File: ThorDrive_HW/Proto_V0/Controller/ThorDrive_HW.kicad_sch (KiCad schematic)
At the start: 33 parts, among them J1 Conn_01x04_Socket, J2 Conn_01x06_Socket, J3 Conn_01x03_Socket, J4 Conn_01x08_Socket, J5 Conn_01x08_Pin, J6 Conn_01x04_Pin, J7 Conn_01x06_Pin, J8 Conn_01x04_Pin, J9 Conn_01x04_Pin, SW1 SW_Push, U1 ATmega328P-P, U4 7400, Y1 Crystal, Y2 Crystal

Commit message: update
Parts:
- C1, C2, C7: footprint (none) -> Capacitor_SMD:C_0805_2012Metric_Pad1.18x1.45mm_HandSolder
- D1, D2, D3, D4, D5, D6: footprint (none) -> LED_SMD:LED_1206_3216Metric_Pad1.42x1.75mm_HandSolder
- R1, R2: footprint (none) -> Resistor_SMD:R_1206_3216Metric_Pad1.30x1.75mm_HandSolder
- R10, R11, R12, R13, R14, R15: footprint (none) -> Resistor_SMD:R_0805_2012Metric_Pad1.20x1.40mm_HandSolder
- U4: footprint (none) -> Package_SO:SOIC-14_3.9x8.7mm_P1.27mm
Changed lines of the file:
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@@
 			)
 		)
-		(property "Footprint" ""
+		(property "Footprint" "Resistor_SMD:R_1206_3216Metric_Pad1.30x1.75mm_HandSolder"
 			(at 92.202 62.23 90)
 			(effects
@@
 			)
 		)
-		(property "Footprint" ""
+		(property "Footprint" "Capacitor_SMD:C_0805_2012Metric_Pad1.18x1.45mm_HandSolder"
 			(at 26.3652 39.37 0)
 			(effects
@@
 			)
 		)
-		(property "Footprint" ""
+		(property "Footprint" "Resistor_SMD:R_0805_2012Metric_Pad1.20x1.40mm_HandSolder"
 			(at 80.772 27.94 90)
 			(effects
@@
 			)
 		)
-		(property "Footprint" ""
+		(property "Footprint" "Capacitor_SMD:C_0805_2012Metric_Pad1.18x1.45mm_HandSolder"
 			(at 134.62 49.8348 0)
 			(effects
@@
 			)
 		)
-		(property "Footprint" ""
+		(property "Footprint" "Package_SO:SOIC-14_3.9x8.7mm_P1.27mm"
 			(at 53.34 154.94 0)
 			(effects
@@
 			)
 		)
-		(property "Footprint" ""
+		(property "Footprint" "LED_SMD:LED_1206_3216Metric_Pad1.42x1.75mm_HandSolder"
 			(at 154.94 43.18 0)
 			(effects
@@
 			)
 		)
-		(property "Footprint" ""
+		(property "Footprint" "Package_SO:SOIC-14_3.9x8.7mm_P1.27mm"
 			(at 53.34 115.57 0)
 			(effects
@@
 			)
 		)
-		(property "Footprint" ""
+		(property "Footprint" "LED_SMD:LED_1206_3216Metric_Pad1.42x1.75mm_HandSolder"
 			(at 161.29 43.18 0)
 			(effects
@@
 			)
 		)
-		(property "Footprint" ""
+		(property "Footprint" "Resistor_SMD:R_1206_3216Metric_Pad1.30x1.75mm_HandSolder"
 			(at 94.742 45.72 90)
 			(effects
@@
 			)
 		)
-		(property "Footprint" ""
+		(property "Footprint" "Resistor_SMD:R_0805_2012Metric_Pad1.20x1.40mm_HandSolder"
 			(at 275.082 39.37 90)
 			(effects
@@
 			)
 		)
-		(property "Footprint" ""
+		(property "Footprint" "LED_SMD:LED_1206_3216Metric_Pad1.42x1.75mm_HandSolder"
 			(at 82.55 35.56 0)
 			(effects
@@
 			)
 		)
-		(property "Footprint" ""
+		(property "Footprint" "Package_SO:SOIC-14_3.9x8.7mm_P1.27mm"
 			(at 53.34 142.24 0)
 			(effects
@@
 			)
 		)
-		(property "Footprint" ""
+		(property "Footprint" "Resistor_SMD:R_0805_2012Metric_Pad1.20x1.40mm_HandSolder"
 			(at 153.162 34.29 90)
 			(effects
@@
 			)
 		)
-		(property "Footprint" ""
+		(property "Footprint" "Capacitor_SMD:C_0805_2012Metric_Pad1.18x1.45mm_HandSolder"
 			(at 134.62 39.6748 0)
 			(effects
@@
 			)
 		)
-		(property "Footprint" ""
+		(property "Footprint" "Resistor_SMD:R_0805_2012Metric_Pad1.20x1.40mm_HandSolder"
 			(at 159.512 34.29 90)
 			(effects
@@
 			)
 		)
-		(property "Footprint" ""
+		(property "Footprint" "Resistor_SMD:R_0805_2012Metric_Pad1.20x1.40mm_HandSolder"
 			(at 159.512 72.39 90)
 			(effects
@@
 			)
 		)
-		(property "Footprint" ""
+		(property "Footprint" "Package_SO:SOIC-14_3.9x8.7mm_P1.27mm"
 			(at 53.34 129.54 0)
 			(effects
@@
 			)
 		)
-		(property "Footprint" ""
+		(property "Footprint" "LED_SMD:LED_1206_3216Metric_Pad1.42x1.75mm_HandSolder"
 			(at 161.29 80.01 0)
 			(effects
@@
 			)
 		)
-		(property "Footprint" ""
+		(property "Footprint" "LED_SMD:LED_1206_3216Metric_Pad1.42x1.75mm_HandSolder"
 			(at 147.32 43.18 0)
 			(effects
@@
 			)
 		)
-		(property "Footprint" ""
+		(property "Footprint" "LED_SMD:LED_1206_3216Metric_Pad1.42x1.75mm_HandSolder"
 			(at 276.86 48.26 0)
 			(effects
@@
 			)
 		)
-		(property "Footprint" ""
+		(property "Footprint" "Resistor_SMD:R_0805_2012Metric_Pad1.20x1.40mm_HandSolder"
 			(at 145.542 34.29 90)
 			(effects
@@
 			)
 		)
-		(property "Footprint" ""
+		(property "Footprint" "Package_SO:SOIC-14_3.9x8.7mm_P1.27mm"
 			(at 261.62 44.45 0)
 			(effects

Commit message: Routing Try0
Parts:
- removed RV1: R_Potentiometer, symbol Device:R_Potentiometer
- added J10: Conn_01x03_Socket, Connector_JST:JST_EH_B3B-EH-A_1x03_P2.50mm_Vertical, symbol Connector:Conn_01x03_Socket
- J1: footprint (none) -> Connector_JST:JST_EH_B4B-EH-A_1x04_P2.50mm_Vertical
- J2: footprint (none) -> Connector_JST:JST_EH_B6B-EH-A_1x06_P2.50mm_Vertical
- J3: footprint (none) -> Connector_JST:JST_EH_B3B-EH-A_1x03_P2.50mm_Vertical
- J4: footprint (none) -> Connector_JST:JST_EH_B8B-EH-A_1x08_P2.50mm_Vertical
- J5: footprint (none) -> Connector_PinHeader_2.54mm:PinHeader_1x08_P2.54mm_Vertical
- J6, J8, J9: footprint (none) -> Connector_PinHeader_2.54mm:PinHeader_1x04_P2.54mm_Vertical
- J7: footprint (none) -> Connector_PinHeader_2.54mm:PinHeader_1x06_P2.54mm_Vertical
- RV2: footprint (none) -> Potentiometer_THT:Potentiometer_Piher_T-16H_Single_Horizontal
- SW1: footprint (none) -> libMain:SW_BUTT-2
- Y1: footprint (none) -> Crystal:Crystal_SMD_HC49-SD_HandSoldering
- Y2: footprint (none) -> Crystal:Crystal_HC49-4H_Vertical
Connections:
- net +5V: now also D2.2 (A), D3.2 (A), D4.2 (A), D5.2 (A), D6.2 (A), J10.3 (Pin_3); no longer R11.1, R12.1, R13.1, R14.1, R15.1
- net Fault: now also R15.2; no longer D6.1 (K)
- net GND: now also R14.2, J10.1 (Pin_1); no longer D5.1 (K)
- net HallA: now also R13.2; no longer D2.1 (K)
- net HallB: now also R12.2; no longer D4.1 (K)
- net HallC: now also R11.2; no longer D3.1 (K)
- net pot: now also J10.2 (Pin_2)
- new net: D4.1 (K), R12.1
- new net: D3.1 (K), R11.1
- new net: D5.1 (K), R14.1
- new net: D6.1 (K), R15.1
- new net: D2.1 (K), R13.1
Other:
- moved on the sheet: D2, D3, D4, D5, D6, R11, R12, R13, R14, R15

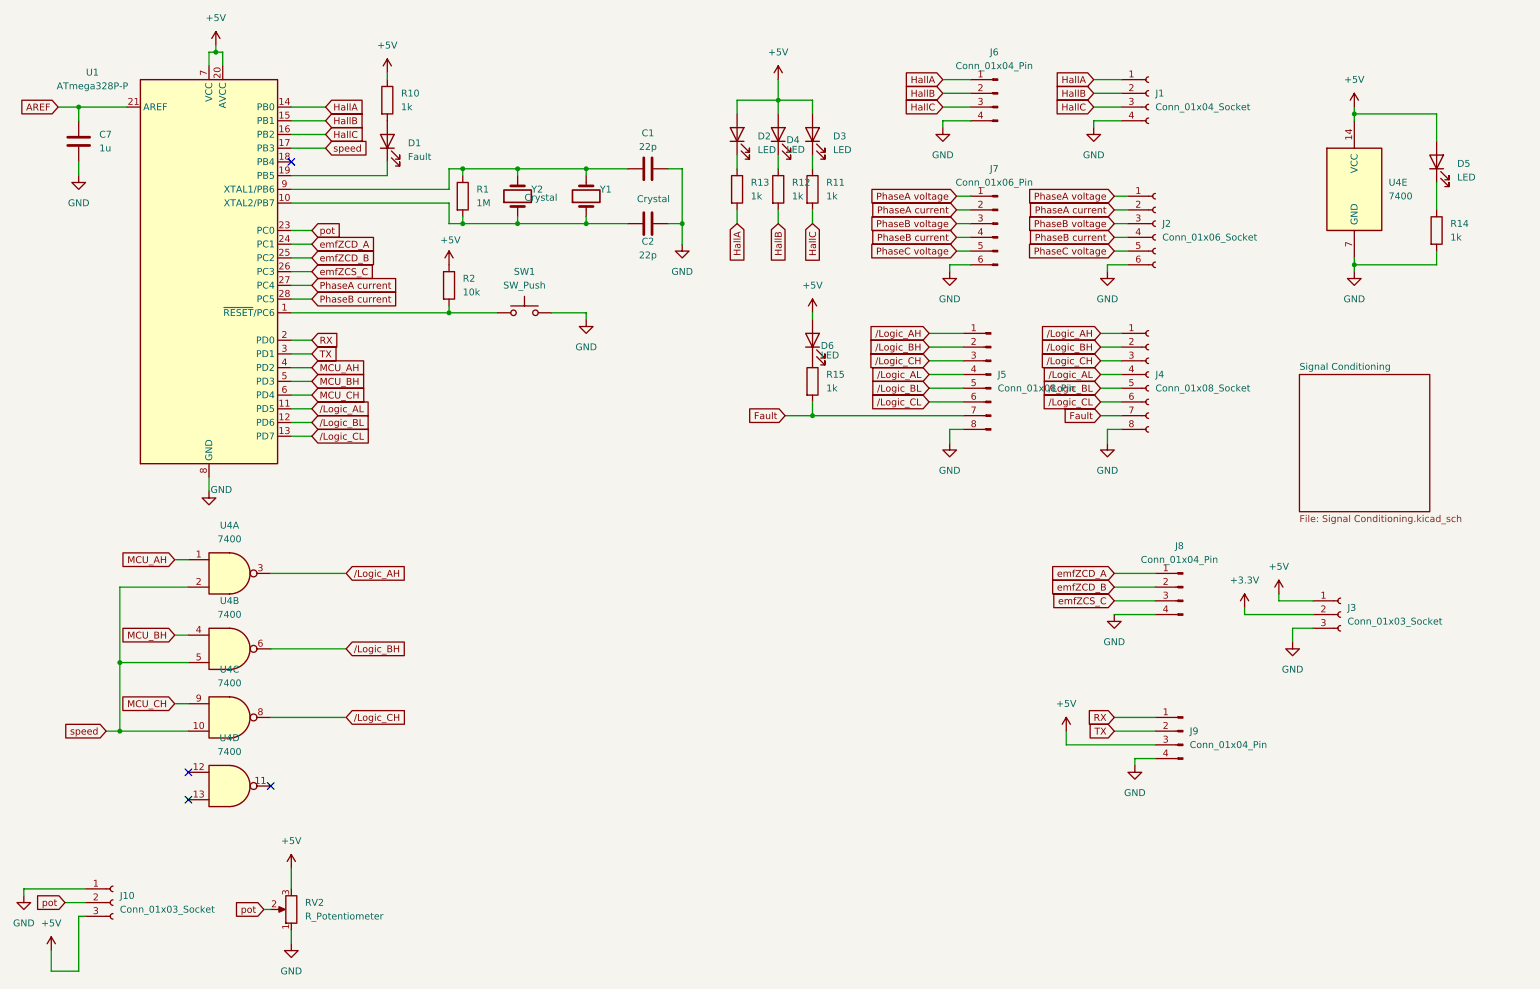
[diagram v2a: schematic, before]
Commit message: Controller Board V0 Finalized
A Controller Board simple and built upon the Atmega328p...
Single Layer Design with few jumpers.... Compatible with Inverter V0
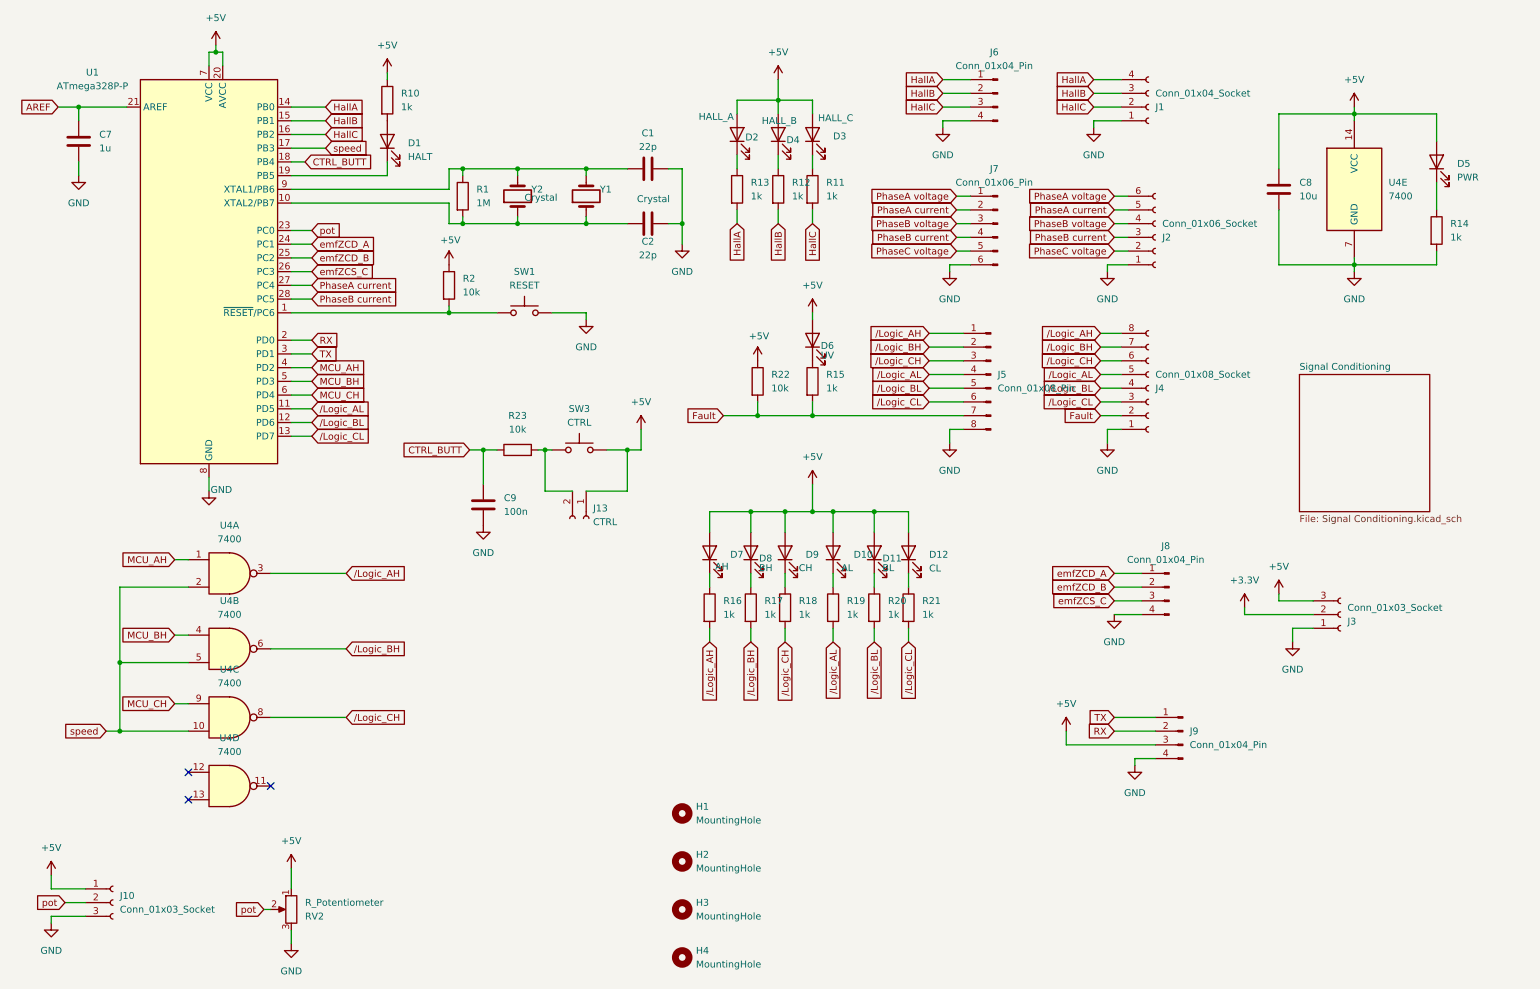
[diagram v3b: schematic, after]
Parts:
- added C8: 10u, Capacitor_SMD:C_0805_2012Metric_Pad1.18x1.45mm_HandSolder, symbol Device:C
- added C9: 100n, Capacitor_SMD:C_0805_2012Metric_Pad1.18x1.45mm_HandSolder, symbol Device:C
- added D10: AL, LED_THT:LED_D3.0mm, symbol Device:LED
- added D11: BL, LED_THT:LED_D3.0mm, symbol Device:LED
- added D12: CL, LED_THT:LED_D3.0mm, symbol Device:LED
- added D7: AH, LED_THT:LED_D3.0mm, symbol Device:LED
- added D8: BH, LED_THT:LED_D3.0mm, symbol Device:LED
- added D9: CH, LED_THT:LED_D3.0mm, symbol Device:LED
- added H1, H2, H3, H4: MountingHole, MountingHole:MountingHole_3.2mm_M3, symbol Mechanical:MountingHole
- added J13: CTRL, Connector_JST:JST_EH_B2B-EH-A_1x02_P2.50mm_Vertical, symbol Connector:Conn_01x02_Socket
- added R16, R17, R18, R19, R20, R21: 1k, Resistor_SMD:R_0805_2012Metric_Pad1.20x1.40mm_HandSolder, symbol Device:R
- added R22, R23: 10k, Resistor_SMD:R_1206_3216Metric_Pad1.30x1.75mm_HandSolder, symbol Device:R
- added SW3: CTRL, libMain:SW_BUTT-2, symbol Switch:SW_Push
- D1: value Fault -> HALT; footprint LED_SMD:LED_1206_3216Metric_Pad1.42x1.75mm_HandSolder -> LED_THT:LED_D3.0mm
- D2: value LED -> HALL_A; footprint LED_SMD:LED_1206_3216Metric_Pad1.42x1.75mm_HandSolder -> LED_THT:LED_D3.0mm
- D3: value LED -> HALL_C; footprint LED_SMD:LED_1206_3216Metric_Pad1.42x1.75mm_HandSolder -> LED_THT:LED_D3.0mm
- D4: value LED -> HALL_B; footprint LED_SMD:LED_1206_3216Metric_Pad1.42x1.75mm_HandSolder -> LED_THT:LED_D3.0mm
- D5: value LED -> PWR; footprint LED_SMD:LED_1206_3216Metric_Pad1.42x1.75mm_HandSolder -> LED_THT:LED_D3.0mm
- D6: value LED -> UV; footprint LED_SMD:LED_1206_3216Metric_Pad1.42x1.75mm_HandSolder -> LED_THT:LED_D3.0mm
- SW1: value SW_Push -> RESET
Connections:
- net +5V: now also J10.1 (Pin_1), J3.3 (Pin_3), RV2.1, C8.1, D10.2 (A), D11.2 (A), D12.2 (A), D7.2 (A), D8.2 (A), D9.2 (A), J13.1 (Pin_1), R22.1, SW3.2; no longer J10.3 (Pin_3), J3.1 (Pin_1), RV2.3
- net Fault: now also J4.2 (Pin_2), R22.2; no longer J4.7 (Pin_7)
- net GND: now also J1.1 (Pin_1), J10.3 (Pin_3), J2.1 (Pin_1), J3.1 (Pin_1), J4.1 (Pin_1), RV2.3, C8.2, C9.2; no longer J1.4 (Pin_4), J10.1 (Pin_1), J2.6 (Pin_6), J3.3 (Pin_3), J4.8 (Pin_8), RV2.1
- net HallA: now also J1.4 (Pin_4); no longer J1.1 (Pin_1)
- net HallB: now also J1.3 (Pin_3); no longer J1.2 (Pin_2)
- net HallC: now also J1.2 (Pin_2); no longer J1.3 (Pin_3)
- net PhaseA current: now also J2.5 (Pin_5); no longer J2.2 (Pin_2)
- net PhaseA voltage: now also J2.6 (Pin_6); no longer J2.1 (Pin_1)
- net PhaseB current: now also J2.3 (Pin_3); no longer J2.4 (Pin_4)
- net PhaseB voltage: now also J2.4 (Pin_4); no longer J2.3 (Pin_3)
- net PhaseC voltage: now also J2.2 (Pin_2); no longer J2.5 (Pin_5)
- net RX: now also J9.2 (Pin_2); no longer J9.1 (Pin_1)
- net TX: now also J9.1 (Pin_1); no longer J9.2 (Pin_2)
- net /Logic_AH: now also J4.8 (Pin_8), R16.2; no longer J4.1 (Pin_1)
- net /Logic_AL: now also J4.5 (Pin_5), R19.2; no longer J4.4 (Pin_4)
- net /Logic_BH: now also J4.7 (Pin_7), R17.2; no longer J4.2 (Pin_2)
- net /Logic_BL: now also J4.4 (Pin_4), R20.2; no longer J4.5 (Pin_5)
- net /Logic_CH: now also J4.6 (Pin_6), R18.2; no longer J4.3 (Pin_3)
- net /Logic_CL: now also J4.3 (Pin_3), R21.2; no longer J4.6 (Pin_6)
- net CTRL_BUTT: now reaches U1.18 (PB4)
- net CTRL_BUTT: now also C9.1, R23.1
- new net: D12.1 (K), R21.1
- new net: D8.1 (K), R17.1
- new net: J13.2 (Pin_2), R23.2, SW3.1
- new net: D9.1 (K), R18.1
- new net: D11.1 (K), R20.1
- new net: D10.1 (K), R19.1
- new net: D7.1 (K), R16.1
- no-connect marks 4 -> 3
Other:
- moved on the sheet: J8, RV2
